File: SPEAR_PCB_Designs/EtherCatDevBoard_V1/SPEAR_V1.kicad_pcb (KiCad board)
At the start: 4 copper layers, 44 x 55 mm, 112 parts, among them J1 USB_C_Receptacle_USB2.0_16P, J2 FTSH-107-01-F-DV-K-P-TR, J3 Conn_01x21_Pin, J4 Conn_01x21_Pin, J5 SM04B-GHS-TB, J6 SM04B-GHS-TB, SW1 SW_Push, T1 H1102NLT, T2 H1102NLT, U1 USBLC6-2SC6, U2 STM32F446RCT6, U3 AMS1117-3.3, U4 LAN9252I/ML, U5 24FC512-I/SN, U6 TPS2116DRL, Y1 16MHz, Y2 25MHz

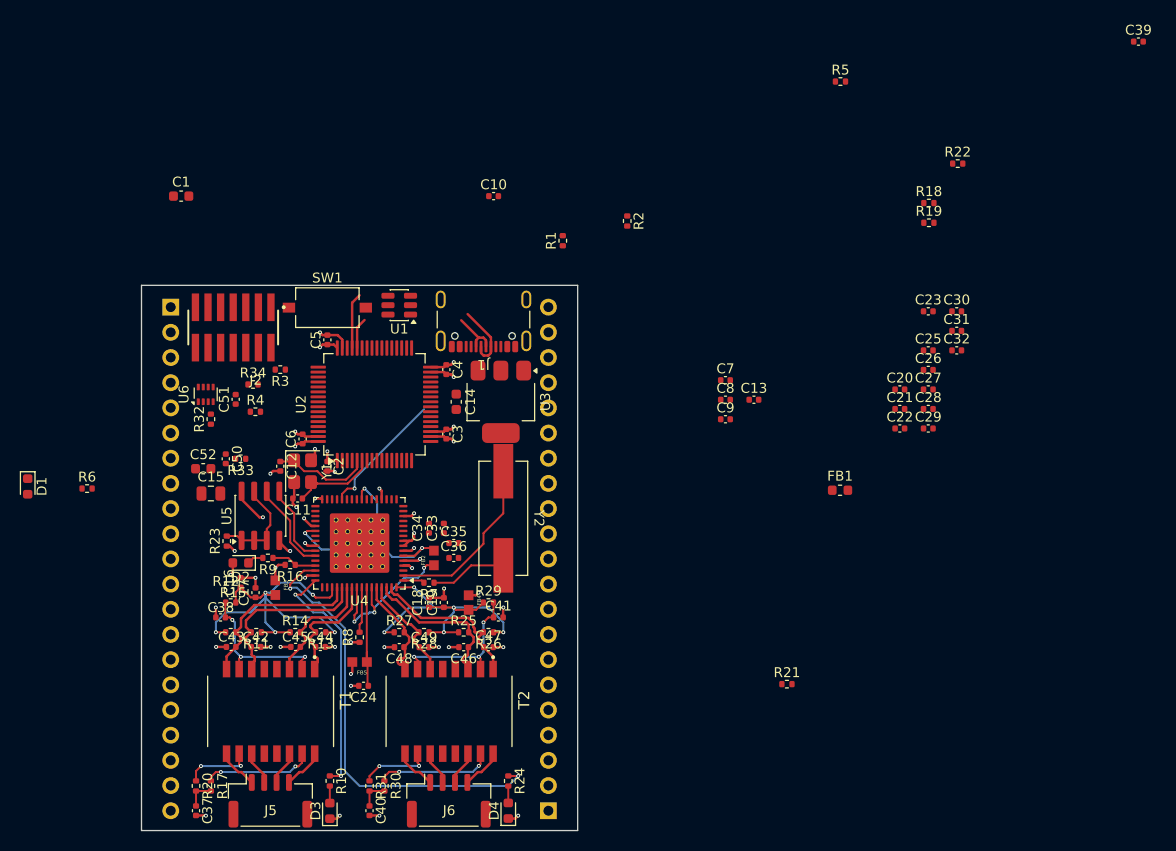
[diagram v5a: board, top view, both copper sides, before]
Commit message: Continued work on the PCB layout of the EtherCAT microcontroller dev board. Not complete yet.
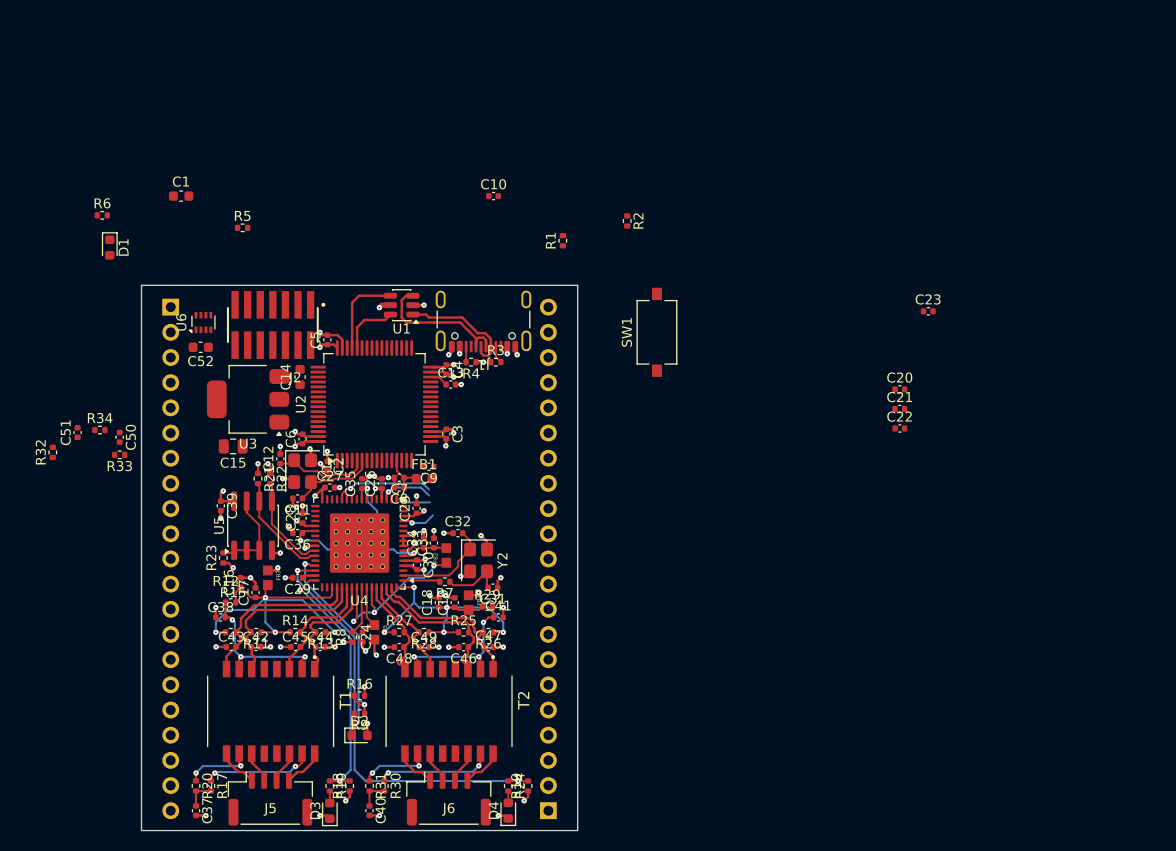
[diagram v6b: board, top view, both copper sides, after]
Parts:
- Y2: footprint LAN9252 Footprints:Y_Wurth_WE-XTAL_Quartz-HC49-4HSMX -> Crystal:Crystal_SMD_Abracon_ABM8G-4Pin_3.2x2.5mm
- moved C39 103.7 mm to (86.0, 124.2), turned to -90 degrees
- moved R18 82.9 mm to (99.0, 152.5), turned to 90 degrees
- moved R22 76.3 mm to (91.0, 121.5), turned to -90 degrees
- moved R19 69.7 mm to (117.0, 152.5), turned to 90 degrees
- moved C29 65.4 mm to (93.8, 131.5), turned to 180 degrees
- moved C28 64.1 mm to (94.2, 125.5), turned to 90 degrees
- moved R5 62.1 mm to (88.2, 96.2)
- moved C27 61.2 mm to (97.0, 122.4)
- moved C30 60.2 mm to (105.8, 130.2), turned to -90 degrees
- moved R21 57.2 mm to (89.8, 121.5), turned to -90 degrees
- moved C26 56.3 mm to (102.2, 122.0), turned to 90 degrees
- moved C25 54.0 mm to (105.8, 124.5), turned to 90 degrees
- moved C32 53.6 mm to (109.9, 127.0)
- moved C31 53.5 mm to (113.5, 132.5), turned to 180 degrees
- moved FB1 42.0 mm to (106.5, 121.5)
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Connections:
- Y2 pad 2: Net-(C31-Pad2) -> GND
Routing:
- net GND: track 46.3 -> 66.4 mm, vias 31 -> 55
- net /LAN9252/GPIO2: track 4.60 -> 22.2 mm, vias 0 -> 2
- net /STM32F446RC/USBC_D+: track 4.98 -> 14.8 mm
- net Net-(U4-OSCO): track 17.6 -> 10.1 mm
- net /STM32F446RC/USBC_D-: track 6.75 -> 13.1 mm
- net +3.3V: track 30.1 -> 36.3 mm, vias 17 -> 19
- net /LAN9252/SCK: track 0.00 -> 5.42 mm, vias 0 -> 1
- net Net-(U4-VDD33BIAS): track 10.7 -> 5.64 mm
- net +3.3VA: track 0.00 -> 4.31 mm
- net /LAN9252/MOSI: track 0.00 -> 3.50 mm, vias 0 -> 1
- net /LAN9252/MISO: track 0.00 -> 3.39 mm, vias 0 -> 1
- net /STM32F446RC/USB_D+: track 5.64 -> 8.73 mm
- net /LAN9252/CS: track 12.9 -> 10.0 mm
- net /STM32F446RC/USB_D-: track 3.14 -> 5.98 mm
- net +5V: track 0.00 -> 2.66 mm, vias 0 -> 3
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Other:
- board text removed: "${REFERENCE}"

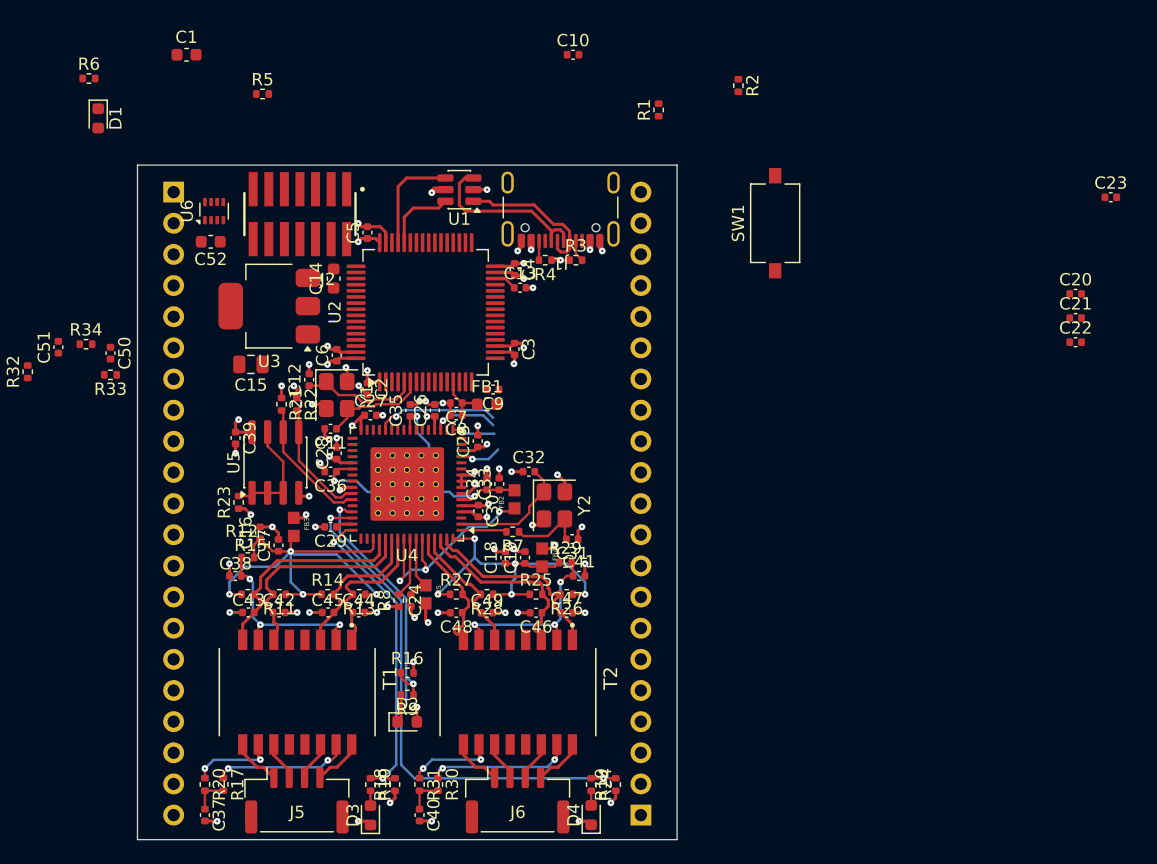
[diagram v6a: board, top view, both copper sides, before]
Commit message: Continued work on EtherCAT microcontroller dev board. Updated it's head pinout.
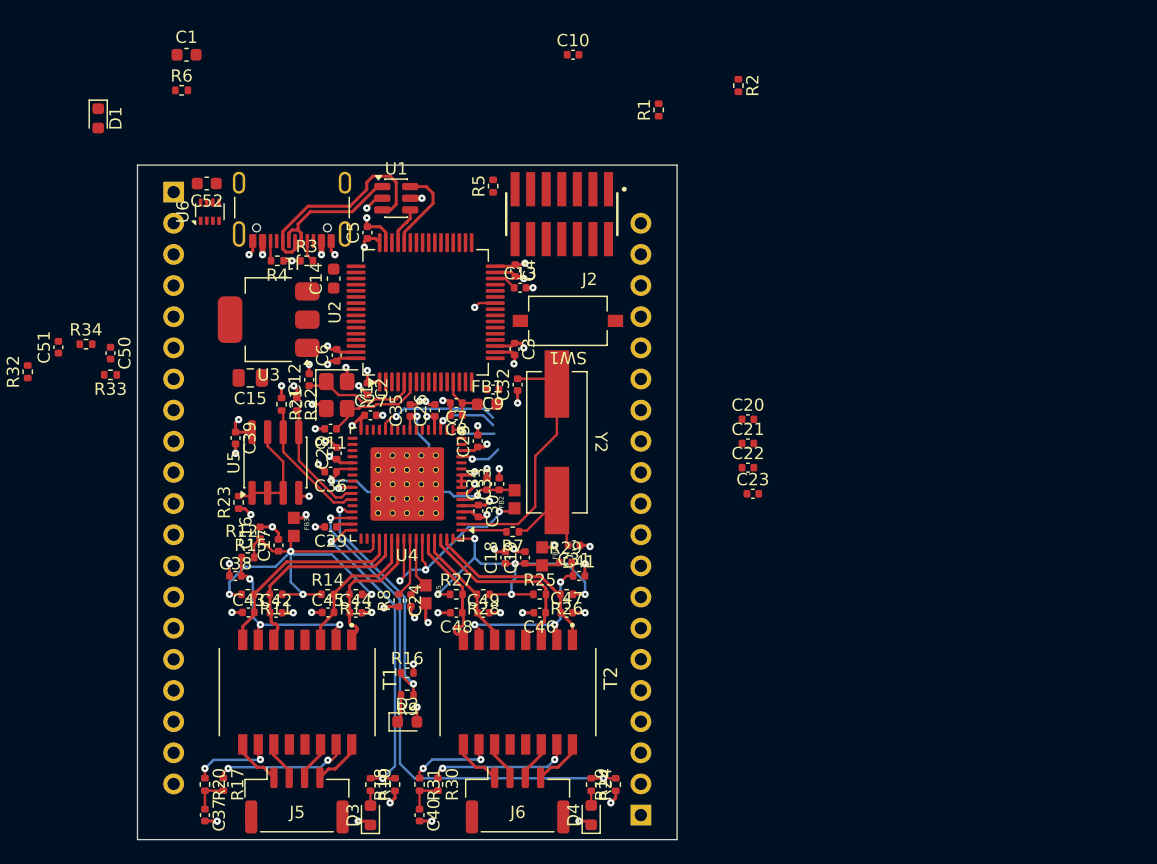
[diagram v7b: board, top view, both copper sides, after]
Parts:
- J3, J4: value Conn_01x21_Pin -> Conn_01x20_Pin; footprint Connector_PinHeader_2.54mm:PinHeader_1x21_P2.54mm_Vertical -> Connector_PinHeader_2.54mm:PinHeader_1x20_P2.54mm_Vertical
- Y2: footprint Crystal:Crystal_SMD_Abracon_ABM8G-4Pin_3.2x2.5mm -> LAN9252 Footprints:Y_Wurth_WE-XTAL_Quartz-HC49-4HSMX
- moved C23 37.9 mm to (128.2, 128.8)
- moved C20 28.6 mm to (127.8, 122.7)
- moved C21 28.6 mm to (127.8, 124.7)
- moved C22 28.6 mm to (127.8, 126.7)
- moved R3 22.0 mm to (91.8, 109.8)
- moved J1 21.9 mm to (90.6, 104.5)
- moved R4 21.9 mm to (89.4, 109.8)
- moved J2 21.3 mm to (112.6, 106.0)
- moved R5 20.2 mm to (107.0, 103.7), turned to 90 degrees
- moved SW1 18.7 mm to (113.1, 114.7), turned to 180 degrees
- moved R6 7.62 mm to (81.6, 95.9)
- moved C32 7.16 mm to (109.0, 119.9), turned to 90 degrees
- moved U1 5.20 mm to (99.1, 104.7), turned to 0 degrees
- moved Y2 5.15 mm to (112.2, 124.6)
- moved C52 4.76 mm to (83.7, 103.5)
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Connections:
- J3 pad 10: /STM32F446RC/PB0 -> /STM32F446RC/PB1
- J3 pad 11: /STM32F446RC/PB1 -> /STM32F446RC/PB2
- J3 pad 12: /STM32F446RC/PB2 -> /STM32F446RC/PB10
- J3 pad 13: /STM32F446RC/PB10 -> /STM32F446RC/PB12
- J3 pad 14: /STM32F446RC/PB12 -> /STM32F446RC/PB13
- J3 pad 15: /STM32F446RC/PB13 -> /STM32F446RC/PB14
- J3 pad 16: /STM32F446RC/PB14 -> /STM32F446RC/PB15
- J3 pad 17: /STM32F446RC/PB15 -> /STM32F446RC/PC9
- J3 pad 18: /STM32F446RC/PC9 -> /STM32F446RC/PC8
- J3 pad 19: /STM32F446RC/PC8 -> /STM32F446RC/PC7
- J3 pad 20: /STM32F446RC/PC7 -> /STM32F446RC/PC6
- J3 pad 8: unconnected-(J3-Pin_8-Pad8) -> /STM32F446RC/PC5
- J3 pad 9: /STM32F446RC/PC5 -> /STM32F446RC/PB0
- U2 pad 4: /STM32F446RC/PC15 -> /LAN9252/IRQ
- Y2 pad 2: GND -> Net-(C31-Pad2)
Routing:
- net Net-(U4-OSCO): track 10.1 -> 20.7 mm
- net /STM32F446RC/USB_D+: track 8.73 -> 3.09 mm
- net /STM32F446RC/USBC_D+: track 14.8 -> 18.1 mm
- net GND: track 66.4 -> 63.7 mm, vias 55 -> 53
- net /STM32F446RC/USBC_D-: track 13.1 -> 11.1 mm
- net /LAN9252/GPIO2: track 22.2 -> 20.2 mm
- net Net-(C31-Pad2): track 6.16 -> 8.18 mm
- net /STM32F446RC/PB0: track 0.00 -> 1.82 mm, vias 0 -> 1
- net /STM32F446RC/USB_D-: track 5.98 -> 7.09 mm
- net /LAN9252/TXA_N: track 17.9 -> 17.0 mm
- net /LAN9252/TXB_N: track 16.4 -> 15.5 mm
- net /LAN9252/TXA_P: track 17.8 -> 17.0 mm
- net /LAN9252/VDDCR: track 27.3 -> 28.0 mm
- net /LAN9252/RXA_N: track 12.5 -> 11.9 mm
- net /LAN9252/RXB_N: track 10.9 -> 10.3 mm
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
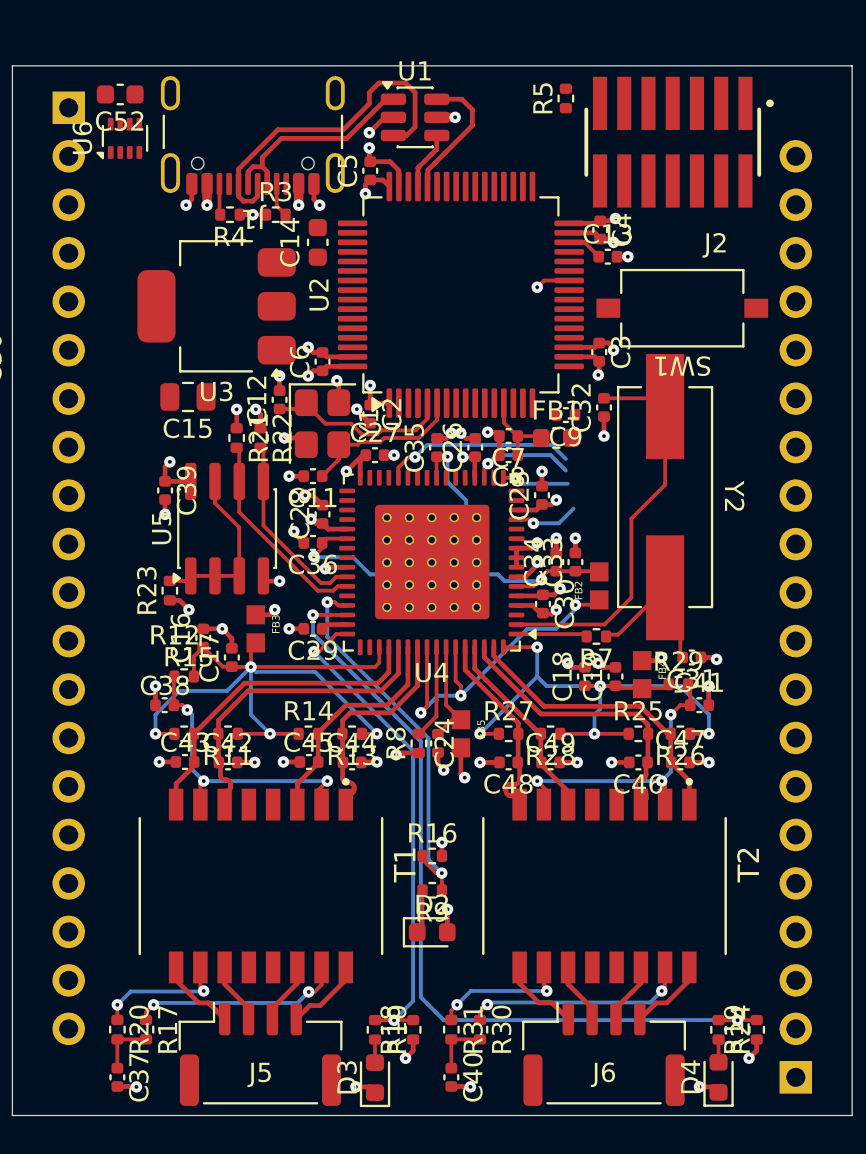
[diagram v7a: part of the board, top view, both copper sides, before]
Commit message: Started adding digikey part ID's to the EtherCAT microcontroller dev. board, but incomplete as of now.
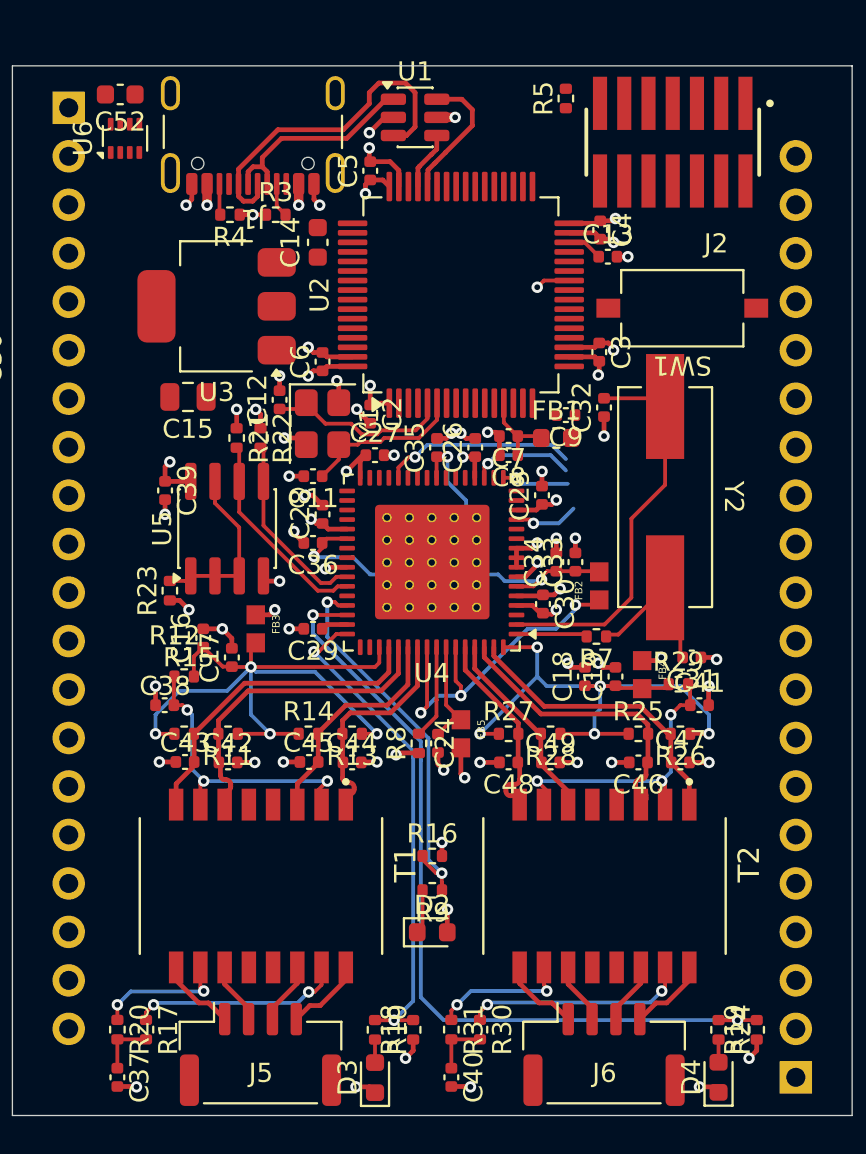
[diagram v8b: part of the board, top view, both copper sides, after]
